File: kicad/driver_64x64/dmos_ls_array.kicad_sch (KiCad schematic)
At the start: 18 parts

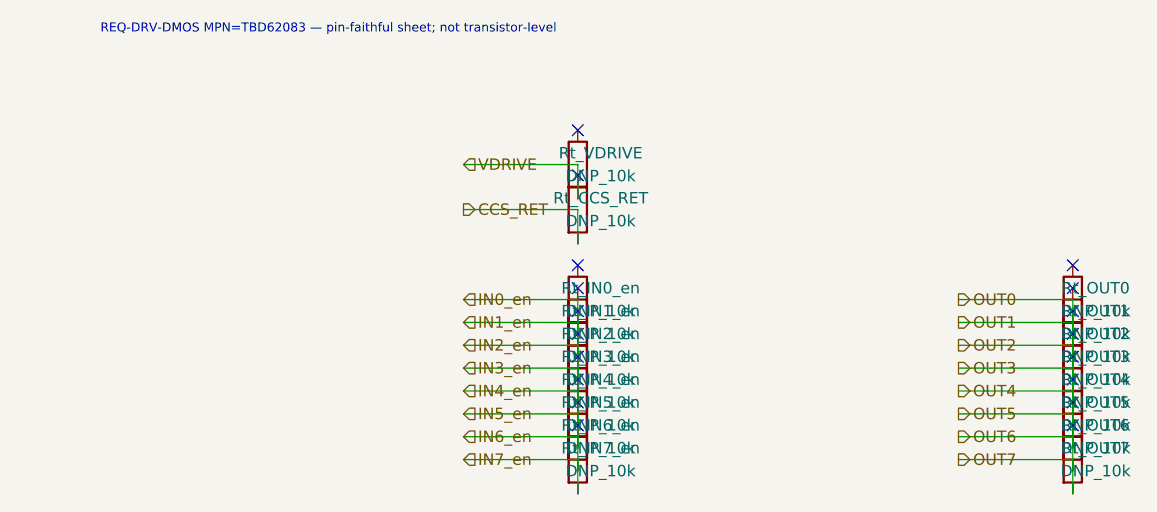
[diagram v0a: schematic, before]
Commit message: logical seperation into host and multiple decode/drive/steering boards
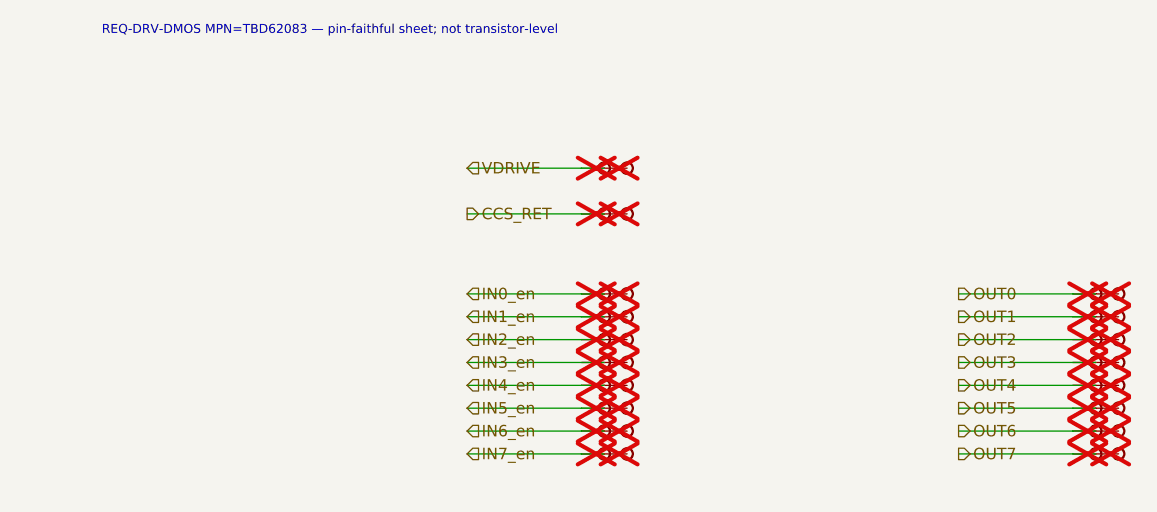
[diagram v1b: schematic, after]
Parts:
- removed Rt_CCS_RET, Rt_IN0_en, Rt_IN1_en, Rt_IN2_en, Rt_IN3_en, Rt_IN4_en, Rt_IN5_en, Rt_IN6_en, Rt_IN7_en, Rt_OUT0, Rt_OUT1, Rt_OUT2, Rt_OUT3, Rt_OUT4, Rt_OUT5, Rt_OUT6, Rt_OUT7, Rt_VDRIVE: DNP_10k, symbol Device:R
- added TP_CCS_RET, TP_CCS_RETb, TP_IN0_en, TP_IN0_enb, TP_IN1_en, TP_IN1_enb, TP_IN2_en, TP_IN2_enb, TP_IN3_en, TP_IN3_enb, TP_IN4_en, TP_IN4_enb, TP_IN5_en, TP_IN5_enb, TP_IN6_en, TP_IN6_enb, TP_IN7_en, TP_IN7_enb, TP_OUT0, TP_OUT0b, TP_OUT1, TP_OUT1b, TP_OUT2, TP_OUT2b, TP_OUT3, TP_OUT3b, TP_OUT4, TP_OUT4b, TP_OUT5, TP_OUT5b, TP_OUT6, TP_OUT6b, TP_OUT7, TP_OUT7b, TP_VDRIVE, TP_VDRIVEb: Stub, symbol CMR:Stub
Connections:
- net CCS_RET: now also TP_CCS_RET.1, TP_CCS_RETb.1
- net IN0_en: now also TP_IN0_en.1, TP_IN0_enb.1
- net OUT0: now also TP_OUT0.1, TP_OUT0b.1
- net VDRIVE: now also TP_VDRIVE.1, TP_VDRIVEb.1
- new net IN1_en: TP_IN1_en.1, TP_IN1_enb.1
- new net IN2_en: TP_IN2_en.1, TP_IN2_enb.1
- new net IN3_en: TP_IN3_en.1, TP_IN3_enb.1
- new net IN4_en: TP_IN4_en.1, TP_IN4_enb.1
- new net IN5_en: TP_IN5_en.1, TP_IN5_enb.1
- new net IN6_en: TP_IN6_en.1, TP_IN6_enb.1
- new net IN7_en: TP_IN7_en.1, TP_IN7_enb.1
- new net OUT1: TP_OUT1.1, TP_OUT1b.1
- new net OUT2: TP_OUT2.1, TP_OUT2b.1
- new net OUT3: TP_OUT3.1, TP_OUT3b.1
- new net OUT4: TP_OUT4.1, TP_OUT4b.1
- new net OUT5: TP_OUT5.1, TP_OUT5b.1
- new net OUT6: TP_OUT6.1, TP_OUT6b.1
- new net OUT7: TP_OUT7.1, TP_OUT7b.1
- no-connect marks 18 -> 0
